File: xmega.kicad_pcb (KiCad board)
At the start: 2 copper layers, 100 x 100 mm, 104 parts, among them J1 USB, J10 AUX, J2 PORTA, J3 PORTB, J4 PORTC, J5 PORTE, J6 PDI, J7 POWER, J8 MCU_CURRENT, J9 RAM_CURRENT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

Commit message: Bugfix: debounce causes bootloader entry on power
Debounce capacitors were connected to ground, which held the IOs low at boot
for about 20ms. Capacitors are now connected to 3.3V instead.
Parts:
- turned C4 to 270 degrees
- turned C5 to 270 degrees
- turned C6 to 270 degrees
- turned C7 to 270 degrees
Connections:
- C4 pad 2: GND -> 3V3MCU
- C5 pad 2: GND -> 3V3MCU
- C6 pad 2: GND -> 3V3MCU
- C7 pad 2: GND -> 3V3MCU
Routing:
- net 3V3MCU: track 239.5 -> 250.9 mm
- net GND: track 559.0 -> 554.5 mm, vias 184 -> 180
- net /UserIO/PF3: track 56.2 -> 55.2 mm
- net /UserIO/PF1: track 37.5 -> 36.7 mm
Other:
- board text added: "CC0 1.0 — REV 2 — 2016-04"
- board text removed: "CC0 1.0 — REV 1 — 2016-03"

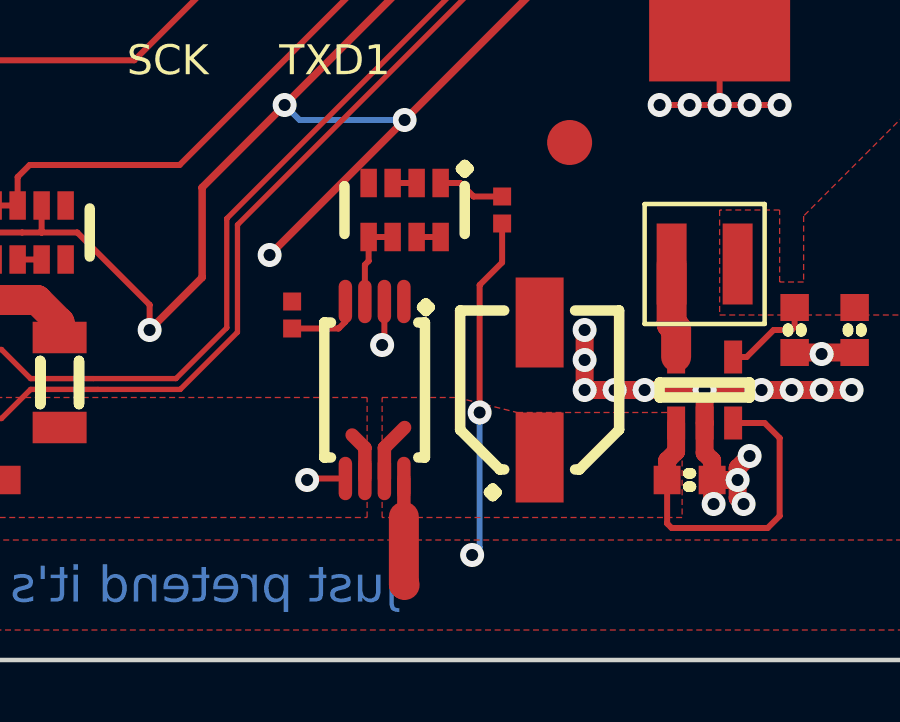
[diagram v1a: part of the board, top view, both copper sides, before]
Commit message: Remove extra resistor R20
With increase of R21 to 15k, it became insignificant - judged better
to remove it and push the power switching threshold a bit lower than
to add another BOM item to increase it.
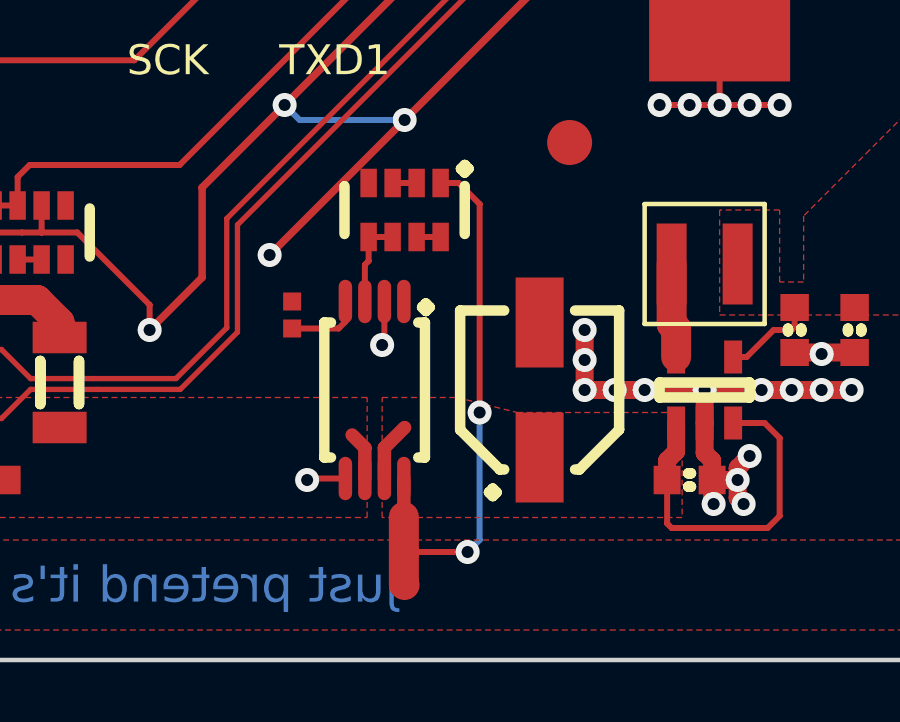
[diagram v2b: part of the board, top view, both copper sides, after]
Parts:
- removed R20: 365, IPC7351-Nominal:RESC1005X40
- C10, C11, C8, C9: value 15p -> 10p
- R15, R21, R23, R9: value 3k3 -> 15k
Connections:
- R21 pad 1: Net-(R20-Pad2) -> /Power/ALT_VBUS_IN
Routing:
- net /Power/ALT_VBUS_IN: track 164.9 -> 168.9 mm
- net Net-(R20-Pad2): track 2.24 -> 0.00 mm

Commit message: Decouple ALT_VBUS locally to U6
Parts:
- added C35: 100n, IPC7351-Nominal:CAPC1005X55, F.Cu at (20.6, 94.6)
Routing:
- net /Power/ALT_VBUS_IN: track 168.9 -> 170.1 mm
- net GND: track 554.5 -> 555.2 mm
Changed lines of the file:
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@@
 (kicad_pcb (version 4) (host pcbnew "(2016-03-30 BZR 6657, Git fe53ec8)-product")
   (general
-    (links 382)
-    (no_connects 1)
+    (links 384)
+    (no_connects 2)
     (area -0.075001 -0.075001 100.075001 100.075001)
     (thickness 1.6)
     (drawings 233)
-    (tracks 2105)
+    (tracks 2108)
     (zones 0)
-    (modules 103)
+    (modules 104)
     (nets 175)
   )
@@
       (net 1 GND))
   )
+  (module IPC7351-Nominal:CAPC1005X55 (layer F.Cu)
+    (at 20.6 94.6 90)
+    (descr "Capacitor,non-polarized,Chip;1.00mm L X 0.50mm W X 0.55mm H")
+    (attr smd)
+    (fp_text reference C35 (at 0 0 180) (layer F.Fab)
+      (effects (font (size 0.8 0.8) (thickness 0.15)))
+    )
+    (fp_text value 100n (at -1.4 0 180) (layer F.Fab)
+      (effects (font (size 0.8 0.8) (thickness 0.15)))
+    )
+    (fp_line (start -1.025 -0.55) (end 1.025 -0.55) (layer F.CrtYd) (width 0.15))
+    (fp_line (start 1.025 -0.55) (end 1.025 0.55) (layer F.CrtYd) (width 0.15))
+    (fp_line (start 1.025 0.55) (end -1.025 0.55) (layer F.CrtYd) (width 0.15))
+    (fp_line (start -1.025 0.55) (end -1.025 -0.55) (layer F.CrtYd) (width 0.15))
+    (pad 1 smd rect (at -0.45 0 90) (size 0.65 0.6) (layers F.Cu F.Paste F.Mask)
+      (net 169 /Power/ALT_VBUS_IN))
+    (pad 2 smd rect (at 0.45 0 90) (size 0.65 0.6) (layers F.Cu F.Paste F.Mask)
+      (net 1 GND))
+    (model smd_cap/c_0402.wrl
+      (at (xyz 0 0 0))
+      (scale (xyz 1 1 1))
+      (rotate (xyz 0 0 0))
+    )
+  )
   (gr_line (start 44 44.5) (end 43.5 44) (layer F.Fab) (width 0.2))
   (gr_line (start 44 43.5) (end 44 44.5) (layer F.Fab) (width 0.2))
@@
   (gr_arc (start 95 5) (end 95 0) (angle 90) (layer Edge.Cuts) (width 0.15))
   (gr_arc (start 5 5) (end 0 5) (angle 90) (layer Edge.Cuts) (width 0.15))
+  (segment (start 21.6 94) (end 20.75 94) (width 0.2) (layer F.Cu) (net 1))
+  (segment (start 20.75 94) (end 20.6 94.15) (width 0.2) (layer F.Cu) (net 1))
+  (via (at 21.6 94) (size 0.8) (drill 0.4) (layers F.Cu B.Cu) (net 1))
+  (segment (start 21.6 94) (end 21.65 93.95) (width 0.2) (layer F.Cu) (net 1))
+  (segment (start 21.65 93.95) (end 22.525 93.95) (width 0.2) (layer F.Cu) (net 1))
   (segment (start 36 81.5) (end 37 81.5) (width 0.2) (layer F.Cu) (net 1))
   (via (at 37 81.5) (size 0.8) (drill 0.4) (layers F.Cu B.Cu) (net 1))
@@
   (via (at 79.250002 10) (size 0.8) (drill 0.4) (layers F.Cu B.Cu) (net 1))
   (segment (start 79.250002 10.000002) (end 79.250002 10) (width 0.25) (layer F.Cu) (net 1))
-  (segment (start 22.525 93.95) (end 21.3 93.95) (width 0.2) (layer F.Cu) (net 1))
-  (segment (start 21.3 93.95) (end 21.25 94) (width 0.2) (layer F.Cu) (net 1))
-  (via (at 21.25 94) (size 0.8) (drill 0.4) (layers F.Cu B.Cu) (net 1))
   (segment (start 23.825 89.175) (end 23.75 89.25) (width 0.2) (layer F.Cu) (net 1))
   (segment (start 23.75 89.25) (end 23.75 89.5) (width 0.2) (layer F.Cu) (net 1))
@@
   (segment (start 29.25 58.25) (end 23.25 58.25) (width 0.2) (layer F.Cu) (net 168))
   (segment (start 23.25 58.25) (end 21.975 59.525) (width 0.2) (layer F.Cu) (net 168))
+  (segment (start 20.6 95.05) (end 20.6 96.2) (width 0.2) (layer F.Cu) (net 169))
   (segment (start 27 84.8) (end 27 91.75) (width 0.2) (layer F.Cu) (net 169))
   (segment (start 27 84.8) (end 26.3 84.1) (width 0.2) (layer F.Cu) (net 169))

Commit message: Switch to passthrough USB TVS
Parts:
- DZ1: value DRTR5V0U2SR -> USBLC6-2SC6; footprint smd-semi:SOT-143 -> smd-semi:SOT-23-6
- moved R23 2.75 mm to (14.2, 87.4)
- moved E1 2.68 mm to (13.4, 93.4)
- moved C13 1.00 mm to (10.5, 95.0)
- moved DZ1 0.21 mm to (9.40, 90.6), turned to 0 degrees
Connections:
- DZ1 pad 1: GND -> /ED-
- DZ1 pad 2: /LD+ -> GND
- DZ1 pad 3: /LD- -> /ED+
- DZ1 pad 4: /E_VBUS -> /LD+
- J1 pad 2: /LD- -> /ED-
- J1 pad 3: /LD+ -> /ED+
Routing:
- net GND: track 555.2 -> 544.9 mm, vias 180 -> 182
- net /LD-: track 67.2 -> 60.1 mm
- net /LD+: track 67.4 -> 60.4 mm
- net /E_VBUS: track 12.4 -> 18.7 mm
- net /ED-: track 0.00 -> 4.39 mm
- net /ED+: track 0.00 -> 4.33 mm
- net Net-(R23-Pad2): track 0.80 -> 2.77 mm

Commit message: Decrease reset pullup
Changing the LED resistors increased it
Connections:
- R9 pad 3: Net-(R9-Pad3) -> 3V3MCU
- R9 pad 4: Net-(R9-Pad3) -> 3V3MCU
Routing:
- net 3V3MCU: track 250.9 -> 253.9 mm
- net Net-(R9-Pad3): track 2.57 -> 0.00 mm
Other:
- board text added: "CC0 1.0 — REV B — 2016-04"
- board text removed: "CC0 1.0 — REV 2 — 2016-04"

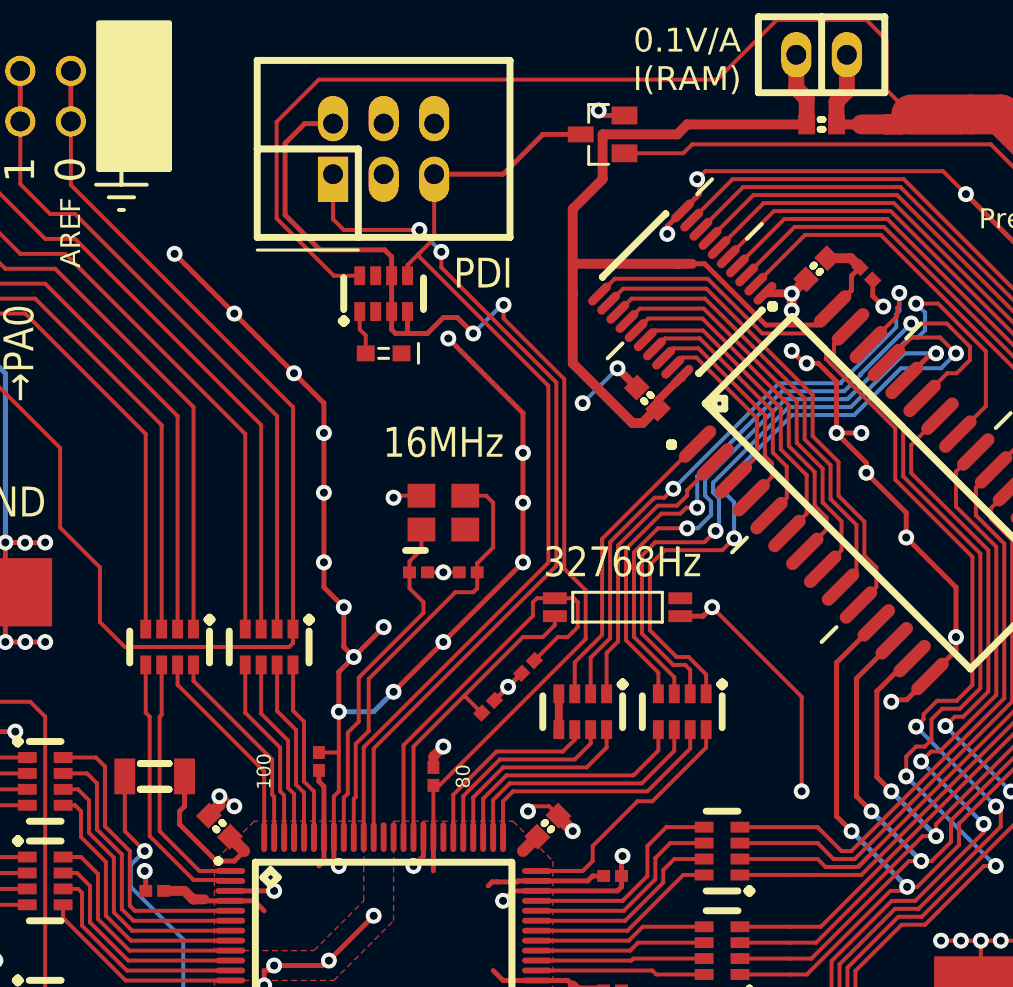
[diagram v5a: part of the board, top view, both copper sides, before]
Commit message: Improved crystal layout
Shorter traces, less coupling between RAM bus and TOSC
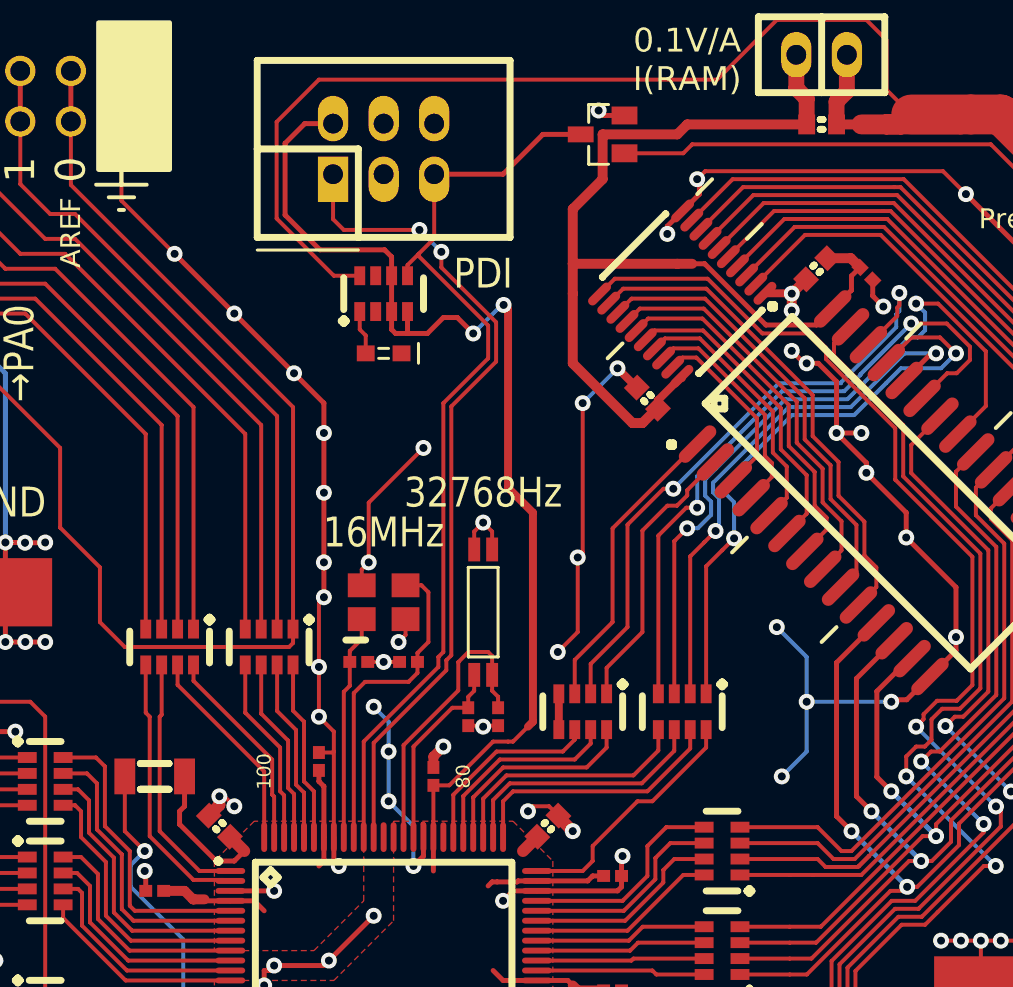
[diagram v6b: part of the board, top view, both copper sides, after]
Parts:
- moved X2 6.75 mm to (55.0, 31.0), turned to 90 degrees
- moved C8 5.41 mm to (48.8, 33.5)
- moved C9 5.41 mm to (51.2, 33.5)
- moved X1 5.41 mm to (50.0, 30.5)
- moved C10 2.92 mm to (55.8, 36.2), turned to 270 degrees
- moved C11 1.12 mm to (54.2, 36.2), turned to 270 degrees
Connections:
- X2 pad 1: /Management/TOSC1 -> /Management/TOSC2
- X2 pad 2: /Management/TOSC2 -> /Management/TOSC1
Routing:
- net GND: track 544.9 -> 557.1 mm, vias 182 -> 184
- net /Management/TOSC2: track 21.0 -> 14.6 mm
- net /Management/XTAL1: track 17.6 -> 11.3 mm
- net /Management/TOSC1: track 15.9 -> 9.88 mm
- net /Management/XTAL2: track 21.8 -> 16.4 mm
- net /RAM/A8: track 34.7 -> 30.3 mm
- net /RAM/A9: track 31.2 -> 27.4 mm
- net /RAM/A10: track 39.4 -> 36.9 mm
- net /Management/PDID: track 44.0 -> 41.5 mm
- net /Management/PDIC: track 49.7 -> 47.2 mm
- net /RAM/A11: track 35.3 -> 33.4 mm
- net 3V3MCU: track 253.9 -> 252.6 mm

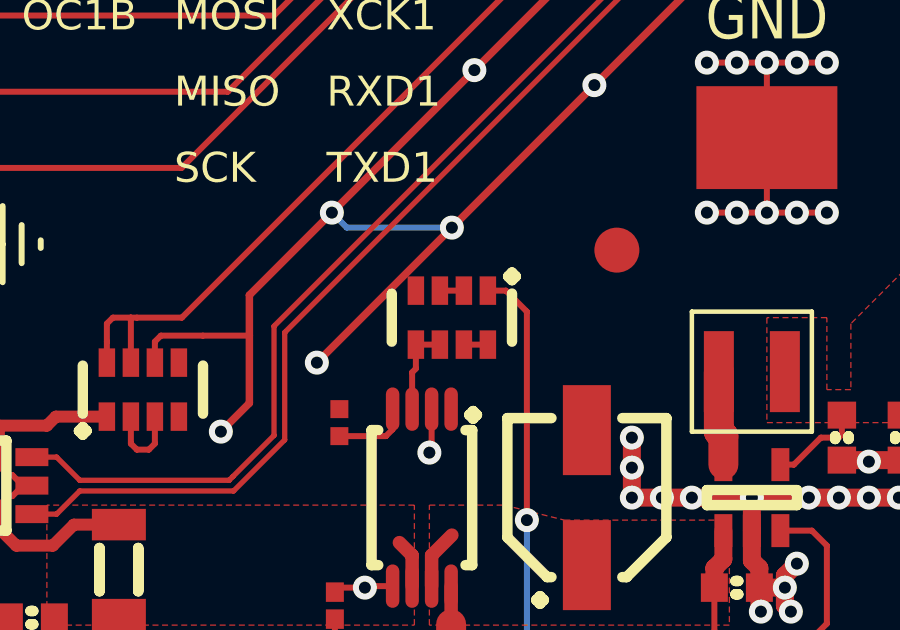
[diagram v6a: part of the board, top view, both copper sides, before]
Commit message: R21: do not link pads under footprint - looks like shorts
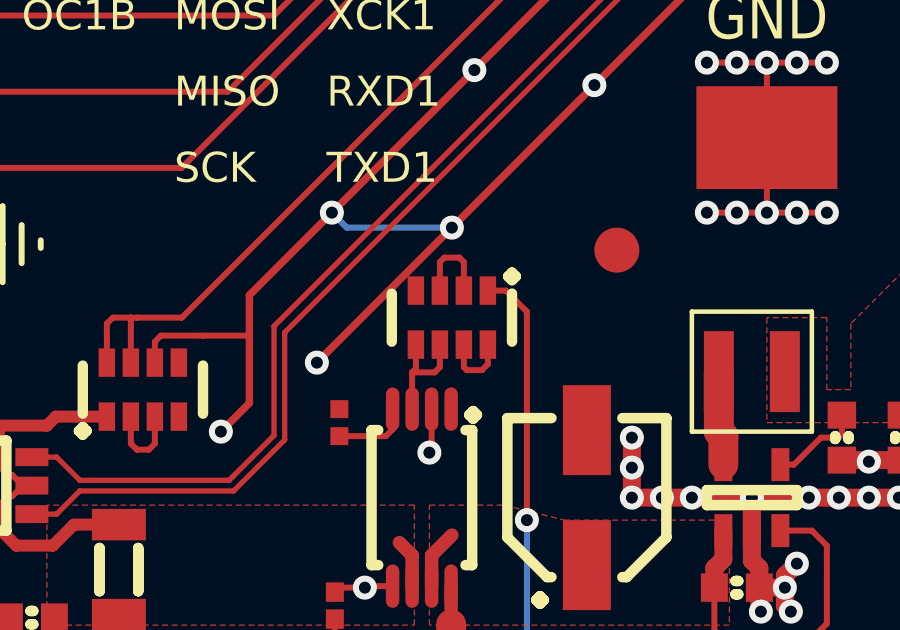
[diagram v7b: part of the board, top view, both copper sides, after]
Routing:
- net Net-(R21-Pad2): track 0.80 -> 2.82 mm
- net Net-(R21-Pad7): track 0.80 -> 2.32 mm
- net Net-(R21-Pad5): track 3.00 -> 3.95 mm
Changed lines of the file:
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@@
   (general
     (links 385)
-    (no_connects 0)
+    (no_connects 2)
     (area -0.075001 -0.075001 100.075001 100.075001)
     (thickness 1.6)
     (drawings 233)
-    (tracks 2103)
+    (tracks 2113)
     (zones 0)
     (modules 104)
@@
   (segment (start 89.5 81.5) (end 90.595 80.405) (width 0.2) (layer F.Cu) (net 157))
   (segment (start 90.595 80.405) (end 92.5 80.405) (width 0.2) (layer F.Cu) (net 157))
-  (segment (start 24.1 84.1) (end 24.9 84.1) (width 0.2) (layer F.Cu) (net 158))
-  (segment (start 24.1 85.9) (end 23.3 85.9) (width 0.2) (layer F.Cu) (net 159))
+  (segment (start 24.75 83) (end 24.9 83.15) (width 0.2) (layer F.Cu) (net 158))
+  (segment (start 24.9 83.15) (end 24.9 84.1) (width 0.2) (layer F.Cu) (net 158))
+  (segment (start 24.25 83) (end 24.75 83) (width 0.2) (layer F.Cu) (net 158))
+  (segment (start 24.1 83.15) (end 24.25 83) (width 0.2) (layer F.Cu) (net 158))
+  (segment (start 24.1 84.1) (end 24.1 83.15) (width 0.2) (layer F.Cu) (net 158))
+  (segment (start 23.925 86.825) (end 24.1 86.65) (width 0.2) (layer F.Cu) (net 159))
+  (segment (start 24.1 86.65) (end 24.1 85.9) (width 0.2) (layer F.Cu) (net 159))
+  (segment (start 23.175 86.825) (end 23.925 86.825) (width 0.2) (layer F.Cu) (net 159))
   (segment (start 23.175 88.05) (end 23.175 86.825) (width 0.2) (layer F.Cu) (net 159))
   (segment (start 23.175 86.825) (end 23.3 86.7) (width 0.2) (layer F.Cu) (net 159))
   (segment (start 23.3 86.7) (end 23.3 85.9) (width 0.2) (layer F.Cu) (net 159))
-  (segment (start 24.9 85.9) (end 25.7 85.9) (width 0.2) (layer F.Cu) (net 160))
+  (segment (start 25.5 86.75) (end 25.7 86.55) (width 0.2) (layer F.Cu) (net 160))
+  (segment (start 25.7 86.55) (end 25.7 85.9) (width 0.2) (layer F.Cu) (net 160))
+  (segment (start 25 86.75) (end 25.5 86.75) (width 0.2) (layer F.Cu) (net 160))
+  (segment (start 24.9 86.65) (end 25 86.75) (width 0.2) (layer F.Cu) (net 160))
+  (segment (start 24.9 85.9) (end 24.9 86.65) (width 0.2) (layer F.Cu) (net 160))
   (segment (start 22.525 88.725) (end 22.3 88.95) (width 0.2) (layer F.Cu) (net 161))
   (segment (start 22.3 88.95) (end 20.75 88.95) (width 0.2) (layer F.Cu) (net 161))
